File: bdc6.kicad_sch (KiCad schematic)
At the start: 3 parts

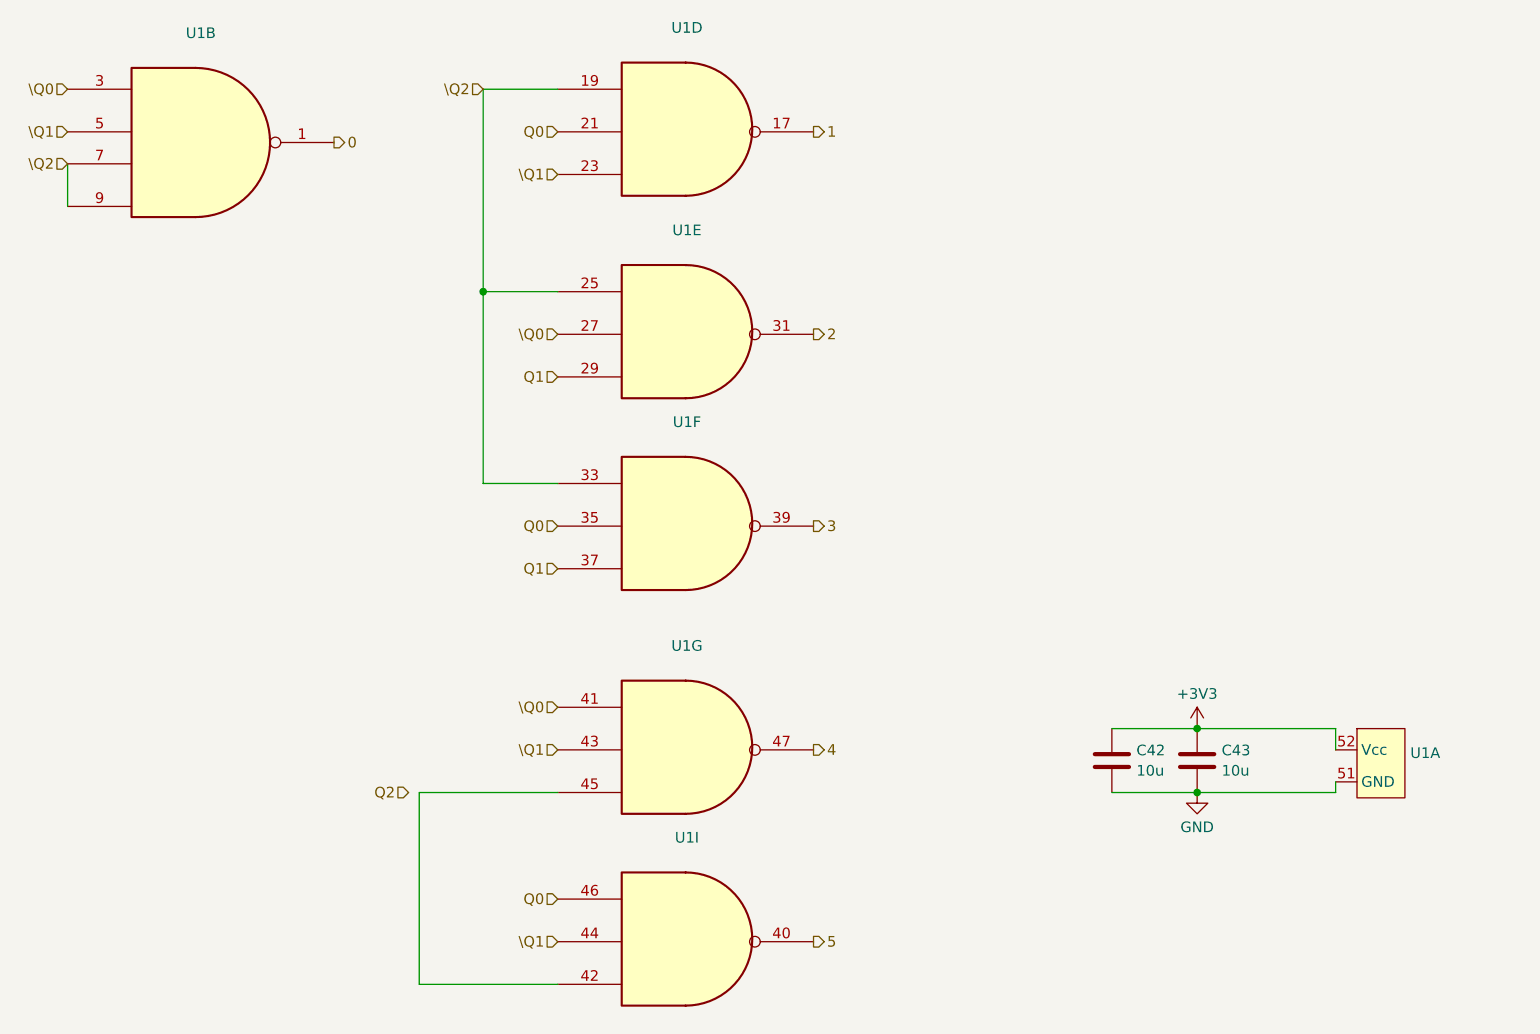
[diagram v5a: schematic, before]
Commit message: added footprints for modules
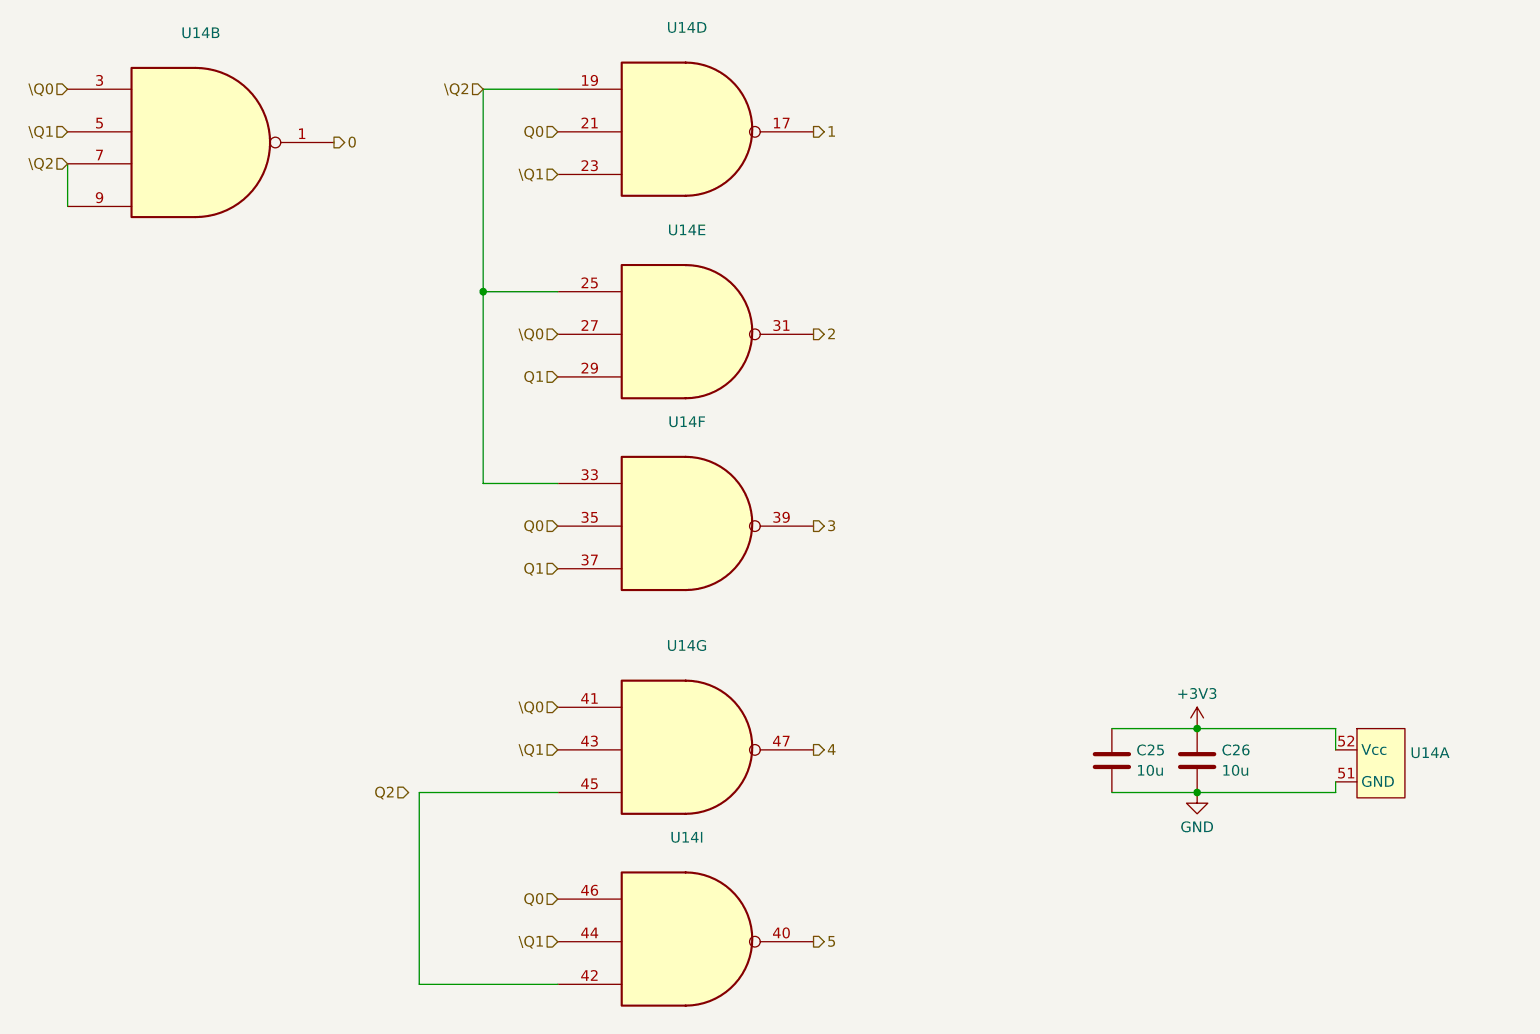
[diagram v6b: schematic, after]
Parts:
- U14: renamed from U1; footprint (none) -> custom:module_bdc_mpcie
- renumbered C42 to C25, C43 to C26
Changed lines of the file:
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@@
 		(dnp no)
 		(fields_autoplaced yes)
-		(property "Reference" "C43"
+		(property "Reference" "C26"
 			(at 168.021 109.2778 0)
 			(effects
@@
 			(project "transistor-clock"
 				(path "/ce10d5bc-995e-4952-aa76-0a08f713a0f2/2c36a9e9-de42-4705-9ad4-94f4cc168e2f/17506e18-a9be-4894-89ef-dc197f5398c9"
-					(reference "C49")
+					(reference "C32")
 					(unit 1)
 				)
 				(path "/ce10d5bc-995e-4952-aa76-0a08f713a0f2/2c36a9e9-de42-4705-9ad4-94f4cc168e2f/d1a94e5b-c816-4015-8ed8-33cd53e200ca"
-					(reference "C43")
+					(reference "C26")
 					(unit 1)
 				)
@@
 		(dnp no)
 		(fields_autoplaced yes)
-		(property "Reference" "U1"
+		(property "Reference" "U14"
 			(at 104.2987 23.1605 0)
 			(effects
@@
 			)
 		)
-		(property "Footprint" ""
+		(property "Footprint" "custom:module_bdc_mpcie"
 			(at 88.9 26.67 0)
 			(effects
@@
 			(project "transistor-clock"
 				(path "/ce10d5bc-995e-4952-aa76-0a08f713a0f2/2c36a9e9-de42-4705-9ad4-94f4cc168e2f/17506e18-a9be-4894-89ef-dc197f5398c9"
-					(reference "U2")
+					(reference "U15")
 					(unit 4)
 				)
 				(path "/ce10d5bc-995e-4952-aa76-0a08f713a0f2/2c36a9e9-de42-4705-9ad4-94f4cc168e2f/d1a94e5b-c816-4015-8ed8-33cd53e200ca"
-					(reference "U1")
+					(reference "U14")
 					(unit 4)
 				)
@@
 		(dnp no)
 		(fields_autoplaced yes)
-		(property "Reference" "C42"
+		(property "Reference" "C25"
 			(at 157.861 109.2778 0)
 			(effects
@@
 			(project "transistor-clock"
 				(path "/ce10d5bc-995e-4952-aa76-0a08f713a0f2/2c36a9e9-de42-4705-9ad4-94f4cc168e2f/17506e18-a9be-4894-89ef-dc197f5398c9"
-					(reference "C48")
+					(reference "C31")
 					(unit 1)
 				)
 				(path "/ce10d5bc-995e-4952-aa76-0a08f713a0f2/2c36a9e9-de42-4705-9ad4-94f4cc168e2f/d1a94e5b-c816-4015-8ed8-33cd53e200ca"
-					(reference "C42")
+					(reference "C25")
 					(unit 1)
 				)
@@
 		(dnp no)
 		(fields_autoplaced yes)
-		(property "Reference" "U1"
+		(property "Reference" "U14"
 			(at 104.2987 119.6805 0)
 			(effects
@@
 			)
 		)
-		(property "Footprint" ""
+		(property "Footprint" "custom:module_bdc_mpcie"
 			(at 87.63 123.19 0)
 			(effects
@@
 			(project "transistor-clock"
 				(path "/ce10d5bc-995e-4952-aa76-0a08f713a0f2/2c36a9e9-de42-4705-9ad4-94f4cc168e2f/17506e18-a9be-4894-89ef-dc197f5398c9"
-					(reference "U2")
+					(reference "U15")
 					(unit 9)
 				)
 				(path "/ce10d5bc-995e-4952-aa76-0a08f713a0f2/2c36a9e9-de42-4705-9ad4-94f4cc168e2f/d1a94e5b-c816-4015-8ed8-33cd53e200ca"
-					(reference "U1")
+					(reference "U14")
 					(unit 9)
 				)
@@
 		(dnp no)
 		(fields_autoplaced yes)
-		(property "Reference" "#PWR0237"
+		(property "Reference" "#PWR044"
 			(at 165.1 120.65 0)
 			(effects
@@
 			(project "transistor-clock"
 				(path "/ce10d5bc-995e-4952-aa76-0a08f713a0f2/2c36a9e9-de42-4705-9ad4-94f4cc168e2f/17506e18-a9be-4894-89ef-dc197f5398c9"
-					(reference "#PWR0243")
+					(reference "#PWR050")
 					(unit 1)
 				)
 				(path "/ce10d5bc-995e-4952-aa76-0a08f713a0f2/2c36a9e9-de42-4705-9ad4-94f4cc168e2f/d1a94e5b-c816-4015-8ed8-33cd53e200ca"
-					(reference "#PWR0237")
+					(reference "#PWR044")
 					(unit 1)
 				)
@@
 		(dnp no)
 		(fields_autoplaced yes)
-		(property "Reference" "#PWR0236"
+		(property "Reference" "#PWR043"
 			(at 165.1 110.49 0)
 			(effects
@@
 			(project "transistor-clock"
 				(path "/ce10d5bc-995e-4952-aa76-0a08f713a0f2/2c36a9e9-de42-4705-9ad4-94f4cc168e2f/17506e18-a9be-4894-89ef-dc197f5398c9"
-					(reference "#PWR0242")
+					(reference "#PWR049")
 					(unit 1)
 				)
 				(path "/ce10d5bc-995e-4952-aa76-0a08f713a0f2/2c36a9e9-de42-4705-9ad4-94f4cc168e2f/d1a94e5b-c816-4015-8ed8-33cd53e200ca"
-					(reference "#PWR0236")
+					(reference "#PWR043")
 					(unit 1)
 				)
@@
 		(dnp no)
 		(fields_autoplaced yes)
-		(property "Reference" "U1"
+		(property "Reference" "U14"
 			(at 190.5 109.5953 0)
 			(effects
@@
 			)
 		)
-		(property "Footprint" ""
+		(property "Footprint" "custom:module_bdc_mpcie"
 			(at 177.8 110.49 0)
 			(effects
@@
 			(project "transistor-clock"
 				(path "/ce10d5bc-995e-4952-aa76-0a08f713a0f2/2c36a9e9-de42-4705-9ad4-94f4cc168e2f/17506e18-a9be-4894-89ef-dc197f5398c9"
-					(reference "U2")
+					(reference "U15")
 					(unit 1)
 				)
 				(path "/ce10d5bc-995e-4952-aa76-0a08f713a0f2/2c36a9e9-de42-4705-9ad4-94f4cc168e2f/d1a94e5b-c816-4015-8ed8-33cd53e200ca"
-					(reference "U1")
+					(reference "U14")
 					(unit 1)
 				)
@@
 		(dnp no)
 		(fields_autoplaced yes)
-		(property "Reference" "U1"
+		(property "Reference" "U14"
 			(at 104.2987 47.2905 0)
 			(effects
@@
 			)
 		)
-		(property "Footprint" ""
+		(property "Footprint" "custom:module_bdc_mpcie"
 			(at 87.63 50.8 0)
 			(effects
@@
 			(project "transistor-clock"
 				(path "/ce10d5bc-995e-4952-aa76-0a08f713a0f2/2c36a9e9-de42-4705-9ad4-94f4cc168e2f/17506e18-a9be-4894-89ef-dc197f5398c9"
-					(reference "U2")
+					(reference "U15")
 					(unit 5)
 				)
 				(path "/ce10d5bc-995e-4952-aa76-0a08f713a0f2/2c36a9e9-de42-4705-9ad4-94f4cc168e2f/d1a94e5b-c816-4015-8ed8-33cd53e200ca"
-					(reference "U1")
+					(reference "U14")
 					(unit 5)
 				)
@@
 		(dnp no)
 		(fields_autoplaced yes)
-		(property "Reference" "U1"
+		(property "Reference" "U14"
 			(at 104.2987 96.8205 0)
 			(effects
@@
 			)
 		)
-		(property "Footprint" ""
+		(property "Footprint" "custom:module_bdc_mpcie"
 			(at 88.9 100.33 0)
 			(effects
@@
 			(project "transistor-clock"
 				(path "/ce10d5bc-995e-4952-aa76-0a08f713a0f2/2c36a9e9-de42-4705-9ad4-94f4cc168e2f/17506e18-a9be-4894-89ef-dc197f5398c9"
-					(reference "U2")
+					(reference "U15")
 					(unit 7)
 				)
 				(path "/ce10d5bc-995e-4952-aa76-0a08f713a0f2/2c36a9e9-de42-4705-9ad4-94f4cc168e2f/d1a94e5b-c816-4015-8ed8-33cd53e200ca"
-					(reference "U1")
+					(reference "U14")
 					(unit 7)
 				)
@@
 		(dnp no)
 		(fields_autoplaced yes)
-		(property "Reference" "U1"
+		(property "Reference" "U14"
 			(at 46.355 23.7955 0)
 			(effects
@@
 			)
 		)
-		(property "Footprint" ""
+		(property "Footprint" "custom:module_bdc_mpcie"
 			(at 36.83 27.94 0)
 			(effects
@@
 			(project "transistor-clock"
 				(path "/ce10d5bc-995e-4952-aa76-0a08f713a0f2/2c36a9e9-de42-4705-9ad4-94f4cc168e2f/17506e18-a9be-4894-89ef-dc197f5398c9"
-					(reference "U2")
+					(reference "U15")
 					(unit 2)
 				)
 				(path "/ce10d5bc-995e-4952-aa76-0a08f713a0f2/2c36a9e9-de42-4705-9ad4-94f4cc168e2f/d1a94e5b-c816-4015-8ed8-33cd53e200ca"
-					(reference "U1")
+					(reference "U14")
 					(unit 2)
 				)
@@
 		(dnp no)
 		(fields_autoplaced yes)
-		(property "Reference" "U1"
+		(property "Reference" "U14"
 			(at 104.2987 70.1505 0)
 			(effects
@@
 			)
 		)
-		(property "Footprint" ""
+		(property "Footprint" "custom:module_bdc_mpcie"
 			(at 87.63 73.66 0)
 			(effects
@@
 			(project "transistor-clock"
 				(path "/ce10d5bc-995e-4952-aa76-0a08f713a0f2/2c36a9e9-de42-4705-9ad4-94f4cc168e2f/17506e18-a9be-4894-89ef-dc197f5398c9"
-					(reference "U2")
+					(reference "U15")
 					(unit 6)
 				)
 				(path "/ce10d5bc-995e-4952-aa76-0a08f713a0f2/2c36a9e9-de42-4705-9ad4-94f4cc168e2f/d1a94e5b-c816-4015-8ed8-33cd53e200ca"
-					(reference "U1")
+					(reference "U14")
 					(unit 6)
 				)

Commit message: added module for PSU
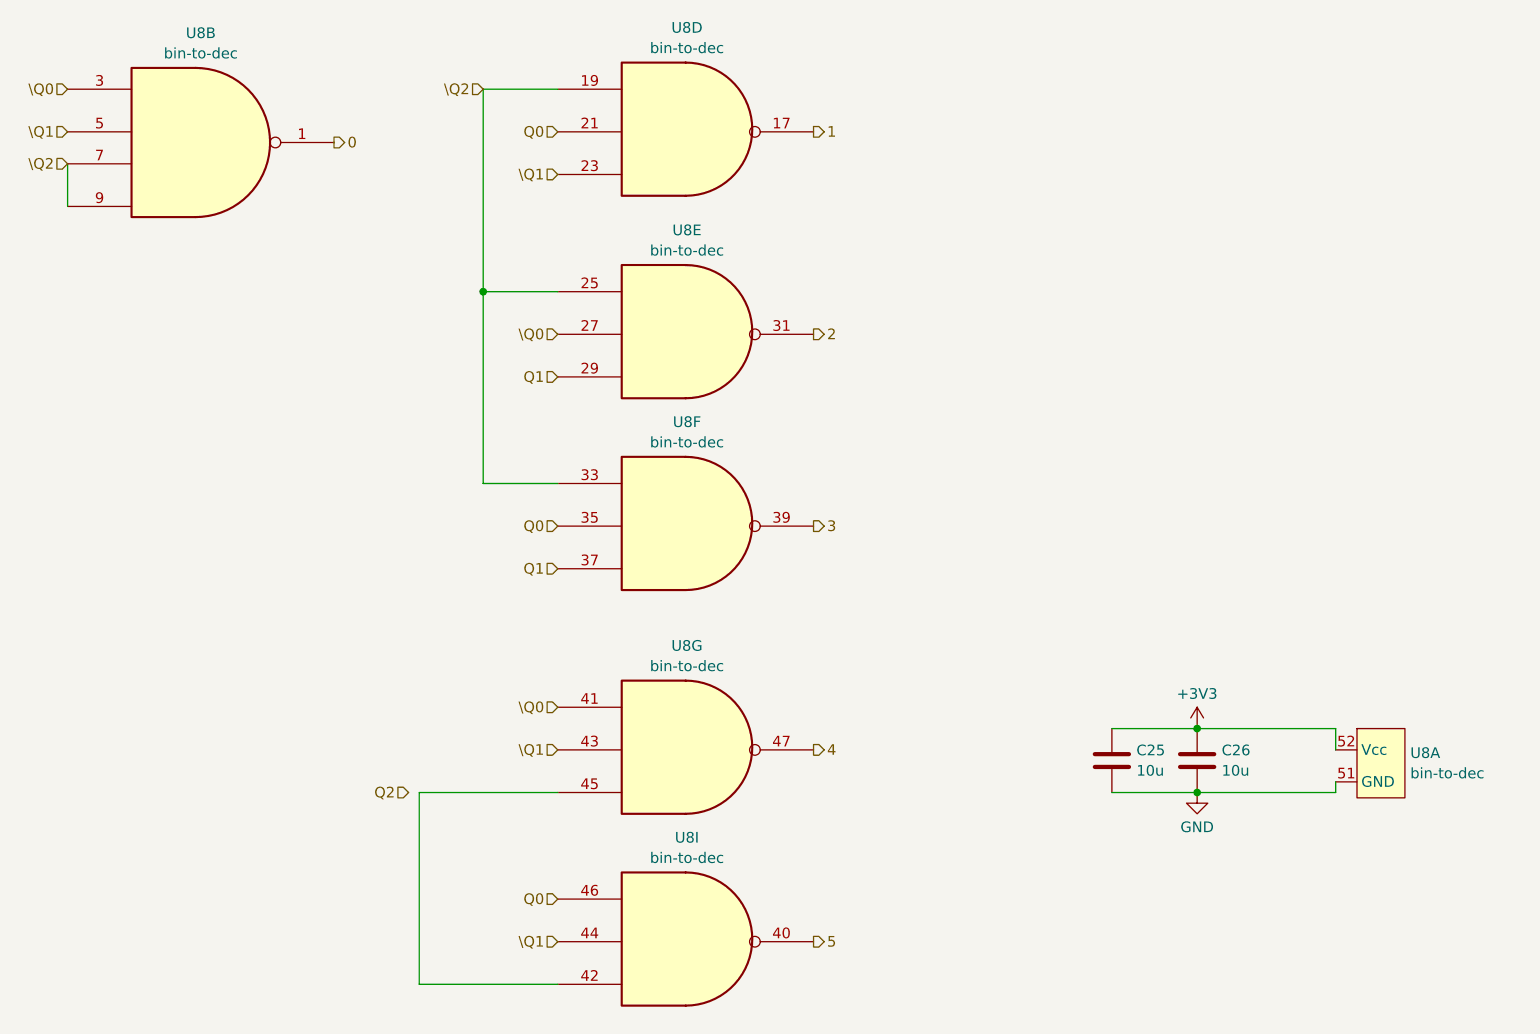
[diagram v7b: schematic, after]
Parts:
- U8: renamed from U14; value ~ -> bin-to-dec; LCSC Part # (none) -> C185937
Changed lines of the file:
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@@
 		(dnp no)
 		(fields_autoplaced yes)
-		(property "Reference" "U14"
+		(property "Reference" "U8"
 			(at 104.2987 23.1605 0)
 			(effects
@@
 			)
 		)
-		(property "Value" "~"
+		(property "Value" "bin-to-dec"
 			(at 104.2987 25.5848 0)
 			(effects
@@
 			)
 		)
-		(property "LCSC Part #" ""
+		(property "LCSC Part #" "C185937"
 			(at 88.9 26.67 0)
 			(effects
@@
 			(project "transistor-clock"
 				(path "/ce10d5bc-995e-4952-aa76-0a08f713a0f2/2c36a9e9-de42-4705-9ad4-94f4cc168e2f/17506e18-a9be-4894-89ef-dc197f5398c9"
-					(reference "U15")
+					(reference "U9")
 					(unit 4)
 				)
 				(path "/ce10d5bc-995e-4952-aa76-0a08f713a0f2/2c36a9e9-de42-4705-9ad4-94f4cc168e2f/d1a94e5b-c816-4015-8ed8-33cd53e200ca"
-					(reference "U14")
+					(reference "U8")
 					(unit 4)
 				)
@@
 		(dnp no)
 		(fields_autoplaced yes)
-		(property "Reference" "U14"
+		(property "Reference" "U8"
 			(at 104.2987 119.6805 0)
 			(effects
@@
 			)
 		)
-		(property "Value" "~"
+		(property "Value" "bin-to-dec"
 			(at 104.2987 122.1048 0)
 			(effects
@@
 			)
 		)
-		(property "LCSC Part #" ""
+		(property "LCSC Part #" "C185937"
 			(at 87.63 123.19 0)
 			(effects
@@
 			(project "transistor-clock"
 				(path "/ce10d5bc-995e-4952-aa76-0a08f713a0f2/2c36a9e9-de42-4705-9ad4-94f4cc168e2f/17506e18-a9be-4894-89ef-dc197f5398c9"
-					(reference "U15")
+					(reference "U9")
 					(unit 9)
 				)
 				(path "/ce10d5bc-995e-4952-aa76-0a08f713a0f2/2c36a9e9-de42-4705-9ad4-94f4cc168e2f/d1a94e5b-c816-4015-8ed8-33cd53e200ca"
-					(reference "U14")
+					(reference "U8")
 					(unit 9)
 				)
@@
 		(dnp no)
 		(fields_autoplaced yes)
-		(property "Reference" "U14"
+		(property "Reference" "U8"
 			(at 190.5 109.5953 0)
 			(effects
@@
 			)
 		)
-		(property "Value" "~"
+		(property "Value" "bin-to-dec"
 			(at 190.5 112.0196 0)
 			(effects
@@
 			)
 		)
-		(property "LCSC Part #" ""
+		(property "LCSC Part #" "C185937"
 			(at 177.8 110.49 0)
 			(effects
@@
 			(project "transistor-clock"
 				(path "/ce10d5bc-995e-4952-aa76-0a08f713a0f2/2c36a9e9-de42-4705-9ad4-94f4cc168e2f/17506e18-a9be-4894-89ef-dc197f5398c9"
-					(reference "U15")
+					(reference "U9")
 					(unit 1)
 				)
 				(path "/ce10d5bc-995e-4952-aa76-0a08f713a0f2/2c36a9e9-de42-4705-9ad4-94f4cc168e2f/d1a94e5b-c816-4015-8ed8-33cd53e200ca"
-					(reference "U14")
+					(reference "U8")
 					(unit 1)
 				)
@@
 		(dnp no)
 		(fields_autoplaced yes)
-		(property "Reference" "U14"
+		(property "Reference" "U8"
 			(at 104.2987 47.2905 0)
 			(effects
@@
 			)
 		)
-		(property "Value" "~"
+		(property "Value" "bin-to-dec"
 			(at 104.2987 49.7148 0)
 			(effects
@@
 			)
 		)
-		(property "LCSC Part #" ""
+		(property "LCSC Part #" "C185937"
 			(at 87.63 50.8 0)
 			(effects
@@
 			(project "transistor-clock"
 				(path "/ce10d5bc-995e-4952-aa76-0a08f713a0f2/2c36a9e9-de42-4705-9ad4-94f4cc168e2f/17506e18-a9be-4894-89ef-dc197f5398c9"
-					(reference "U15")
+					(reference "U9")
 					(unit 5)
 				)
 				(path "/ce10d5bc-995e-4952-aa76-0a08f713a0f2/2c36a9e9-de42-4705-9ad4-94f4cc168e2f/d1a94e5b-c816-4015-8ed8-33cd53e200ca"
-					(reference "U14")
+					(reference "U8")
 					(unit 5)
 				)
@@
 		(dnp no)
 		(fields_autoplaced yes)
-		(property "Reference" "U14"
+		(property "Reference" "U8"
 			(at 104.2987 96.8205 0)
 			(effects
@@
 			)
 		)
-		(property "Value" "~"
+		(property "Value" "bin-to-dec"
 			(at 104.2987 99.2448 0)
 			(effects
@@
 			)
 		)
-		(property "LCSC Part #" ""
+		(property "LCSC Part #" "C185937"
 			(at 88.9 100.33 0)
 			(effects
@@
 			(project "transistor-clock"
 				(path "/ce10d5bc-995e-4952-aa76-0a08f713a0f2/2c36a9e9-de42-4705-9ad4-94f4cc168e2f/17506e18-a9be-4894-89ef-dc197f5398c9"
-					(reference "U15")
+					(reference "U9")
 					(unit 7)
 				)
 				(path "/ce10d5bc-995e-4952-aa76-0a08f713a0f2/2c36a9e9-de42-4705-9ad4-94f4cc168e2f/d1a94e5b-c816-4015-8ed8-33cd53e200ca"
-					(reference "U14")
+					(reference "U8")
 					(unit 7)
 				)
@@
 		(dnp no)
 		(fields_autoplaced yes)
-		(property "Reference" "U14"
+		(property "Reference" "U8"
 			(at 46.355 23.7955 0)
 			(effects
@@
 			)
 		)
-		(property "Value" "~"
+		(property "Value" "bin-to-dec"
 			(at 46.355 26.2198 0)
 			(effects
@@
 			)
 		)
-		(property "LCSC Part #" ""
+		(property "LCSC Part #" "C185937"
 			(at 36.83 27.94 0)
 			(effects
@@
 			(project "transistor-clock"
 				(path "/ce10d5bc-995e-4952-aa76-0a08f713a0f2/2c36a9e9-de42-4705-9ad4-94f4cc168e2f/17506e18-a9be-4894-89ef-dc197f5398c9"
-					(reference "U15")
+					(reference "U9")
 					(unit 2)
 				)
 				(path "/ce10d5bc-995e-4952-aa76-0a08f713a0f2/2c36a9e9-de42-4705-9ad4-94f4cc168e2f/d1a94e5b-c816-4015-8ed8-33cd53e200ca"
-					(reference "U14")
+					(reference "U8")
 					(unit 2)
 				)
@@
 		(dnp no)
 		(fields_autoplaced yes)
-		(property "Reference" "U14"
+		(property "Reference" "U8"
 			(at 104.2987 70.1505 0)
 			(effects
@@
 			)
 		)
-		(property "Value" "~"
+		(property "Value" "bin-to-dec"
 			(at 104.2987 72.5748 0)
 			(effects
@@
 			)
 		)
-		(property "LCSC Part #" ""
+		(property "LCSC Part #" "C185937"
 			(at 87.63 73.66 0)
 			(effects
@@
 			(project "transistor-clock"
 				(path "/ce10d5bc-995e-4952-aa76-0a08f713a0f2/2c36a9e9-de42-4705-9ad4-94f4cc168e2f/17506e18-a9be-4894-89ef-dc197f5398c9"
-					(reference "U15")
+					(reference "U9")
 					(unit 6)
 				)
 				(path "/ce10d5bc-995e-4952-aa76-0a08f713a0f2/2c36a9e9-de42-4705-9ad4-94f4cc168e2f/d1a94e5b-c816-4015-8ed8-33cd53e200ca"
-					(reference "U14")
+					(reference "U8")
 					(unit 6)
 				)

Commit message: routy mcRouteface
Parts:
- C25, C26: LCSC Part # C57112 -> C19702
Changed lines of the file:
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@@
 			)
 		)
-		(property "LCSC Part #" "C57112"
+		(property "LCSC Part #" "C19702"
 			(at 165.1 110.49 0)
 			(effects
@@
 			)
 		)
-		(property "LCSC Part #" "C57112"
+		(property "LCSC Part #" "C19702"
 			(at 154.94 110.49 0)
 			(effects
